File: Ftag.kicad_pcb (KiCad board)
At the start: 2 copper layers, 34.9 x 29.2 mm, 25 parts, among them P1 USB_OTG, P2 CONN_10X2, U1 FT232H, U2 TXB0108, X1 12 MHz

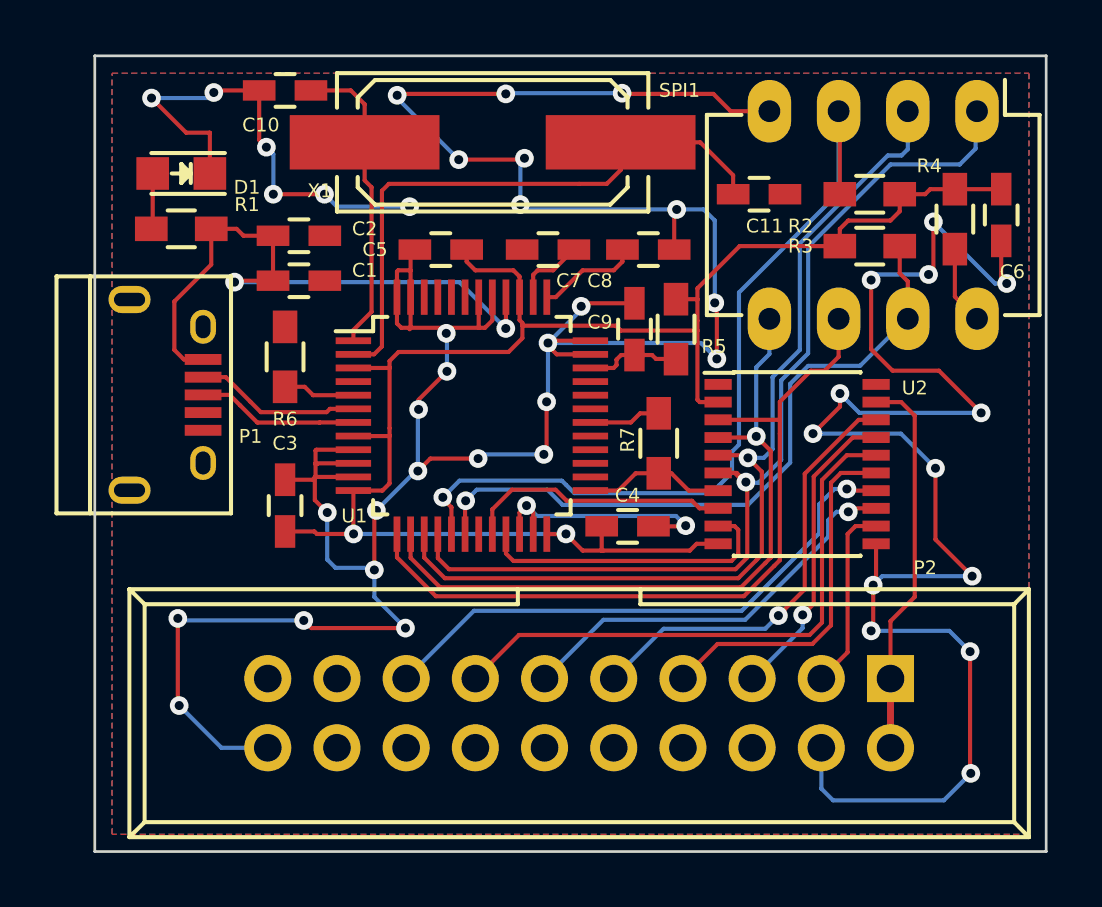
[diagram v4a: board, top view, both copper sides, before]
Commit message: Finished PCB layout
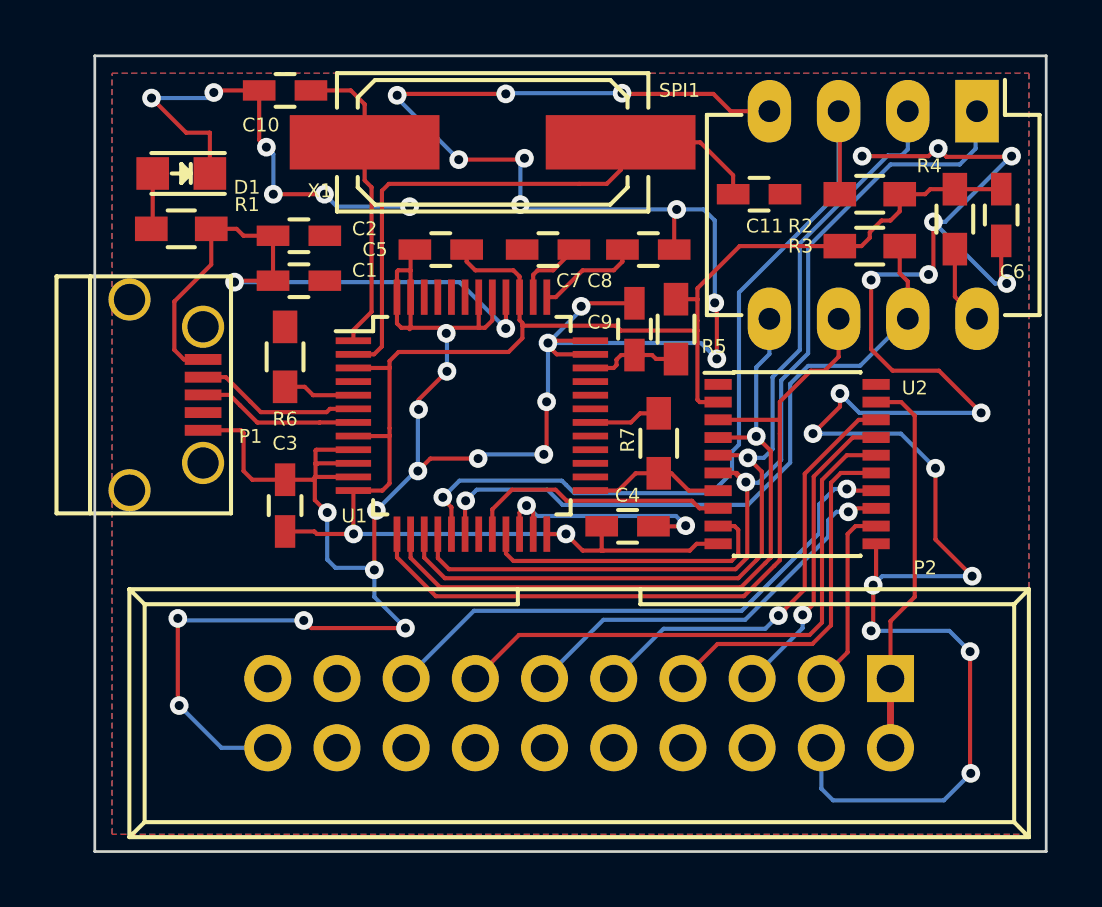
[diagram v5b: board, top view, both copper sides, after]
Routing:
- net GND: track 197.5 -> 211.7 mm, vias 46 -> 49
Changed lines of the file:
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@@
     (thickness 1.6)
     (drawings 17)
-    (tracks 542)
+    (tracks 562)
     (zones 0)
     (modules 25)
@@
     (mod_text_size 1 1)
     (mod_text_width 0.15)
-    (pad_size 5.4991 1.99898)
-    (pad_drill 0)
+    (pad_size 2.3 1.6)
+    (pad_drill 0.8)
     (pad_to_mask_clearance 0)
     (aux_axis_origin 0 0)
-    (visible_elements FFFFFFFF)
+    (visible_elements FFFFFF7F)
     (pcbplotparams
       (layerselection 0x010f0_80000001)
@@
     (pad 5 smd rect (at 1.2991 -1.56254) (size 1.35 0.4) (layers F.Cu F.Paste F.Mask)
       (net 2 GND))
-    (pad 6 thru_hole oval (at -2.5009 -1.56254) (size 0.95 1.25) (drill oval 0.55 0.85) (layers *.Cu *.Mask F.SilkS)
-      (net 2 GND))
-    (pad 6 thru_hole oval (at 2.4991 -1.56254) (size 0.95 1.25) (drill oval 0.55 0.85) (layers *.Cu *.Mask F.SilkS)
-      (net 2 GND))
-    (pad 6 thru_hole oval (at -3.5009 1.13746) (size 1.55 1) (drill oval 1.15 0.5) (layers *.Cu *.Mask F.SilkS)
-      (net 2 GND))
-    (pad 6 thru_hole oval (at 3.4991 1.13746) (size 1.55 1) (drill oval 1.15 0.5) (layers *.Cu *.Mask F.SilkS)
+    (pad 6 thru_hole circle (at -2.5009 -1.56254) (size 1.55 1.55) (drill 1.15) (layers *.Cu *.Mask F.SilkS)
+      (net 2 GND))
+    (pad 6 thru_hole circle (at 2.4991 -1.56254) (size 1.55 1.55) (drill 1.15) (layers *.Cu *.Mask F.SilkS)
+      (net 2 GND))
+    (pad 6 thru_hole circle (at -3.5009 1.13746) (size 1.55 1.55) (drill 1.15) (layers *.Cu *.Mask F.SilkS)
+      (net 2 GND))
+    (pad 6 thru_hole circle (at 3.4991 1.13746) (size 1.55 1.55) (drill 1.15) (layers *.Cu *.Mask F.SilkS)
       (net 2 GND))
   )
@@
     (fp_line (start 0.135 9.915) (end 7.485 9.915) (layer F.SilkS) (width 0.15))
     (fp_line (start 0.135 -1.025) (end -1.15 -1.025) (layer F.SilkS) (width 0.15))
-    (pad 1 thru_hole oval (at 0 0 270) (size 2.3 1.6) (drill 0.8) (layers *.Cu *.Mask F.SilkS)
+    (pad 1 thru_hole rect (at 0 0 270) (size 2.3 1.6) (drill 0.8) (layers *.Cu *.Mask F.SilkS)
       (net 24 /CTS/TMS/CS))
     (pad 2 thru_hole oval (at 0 2.54 270) (size 2.3 1.6) (drill 0.8) (layers *.Cu *.Mask F.SilkS)
@@
   (segment (start 148.336 75.184) (end 148.082 74.93) (width 0.1524) (layer F.Cu) (net 1))
   (segment (start 149.418 76.835) (end 149.418 75.184) (width 0.1524) (layer F.Cu) (net 1))
+  (segment (start 173.8376 71.9836) (end 173.7614 71.9836) (width 0.1524) (layer F.Cu) (net 2))
+  (via (at 171.0436 72.263) (size 0.6858) (drill 0.3302) (layers F.Cu B.Cu) (net 2))
+  (segment (start 173.482 72.263) (end 171.0436 72.263) (width 0.1524) (layer F.Cu) (net 2))
+  (segment (start 173.7614 71.9836) (end 173.482 72.263) (width 0.1524) (layer F.Cu) (net 2))
+  (segment (start 173.6598 74.676) (end 174.0916 74.676) (width 0.1524) (layer B.Cu) (net 2))
+  (segment (start 173.8376 71.9836) (end 173.8376 71.9582) (width 0.1524) (layer B.Cu) (net 2))
+  (via (at 173.8376 71.9836) (size 0.6858) (drill 0.3302) (layers F.Cu B.Cu) (net 2))
+  (segment (start 174.1424 72.2884) (end 173.8376 71.9836) (width 0.1524) (layer F.Cu) (net 2))
+  (segment (start 176.5046 72.2884) (end 174.1424 72.2884) (width 0.1524) (layer F.Cu) (net 2))
+  (segment (start 176.53 72.263) (end 176.5046 72.2884) (width 0.1524) (layer F.Cu) (net 2))
+  (via (at 176.53 72.263) (size 0.6858) (drill 0.3302) (layers F.Cu B.Cu) (net 2))
+  (segment (start 176.5046 72.263) (end 176.53 72.263) (width 0.1524) (layer B.Cu) (net 2))
+  (segment (start 174.0916 74.676) (end 176.5046 72.263) (width 0.1524) (layer B.Cu) (net 2))
+  (segment (start 152.368 83.038) (end 151.0084 83.038) (width 0.1524) (layer F.Cu) (net 2))
+  (segment (start 151.0084 83.038) (end 150.9776 83.0688) (width 0.1524) (layer F.Cu) (net 2))
+  (segment (start 150.9776 83.0688) (end 150.9776 83.566) (width 0.1524) (layer F.Cu) (net 2))
+  (segment (start 146.85054 82.3251) (end 148.2381 82.3251) (width 0.1524) (layer F.Cu) (net 2))
+  (segment (start 148.656 84.14) (end 149.86 84.14) (width 0.1524) (layer F.Cu) (net 2))
+  (segment (start 148.336 83.82) (end 148.656 84.14) (width 0.1524) (layer F.Cu) (net 2))
+  (segment (start 148.336 82.423) (end 148.336 83.82) (width 0.1524) (layer F.Cu) (net 2))
+  (segment (start 148.2381 82.3251) (end 148.336 82.423) (width 0.1524) (layer F.Cu) (net 2))
   (via (at 175.4124 81.6864) (size 0.6858) (drill 0.3302) (layers F.Cu B.Cu) (net 2))
   (via (at 175.0822 87.6808) (size 0.6858) (drill 0.3302) (layers F.Cu B.Cu) (net 2))
@@
   (segment (start 150.9522 84.038) (end 150.9882 84.038) (width 0.1524) (layer F.Cu) (net 2))
   (segment (start 150.9882 84.038) (end 150.9776 84.0486) (width 0.1524) (layer F.Cu) (net 2))
-  (segment (start 152.368 83.038) (end 151.0084 83.038) (width 0.1524) (layer F.Cu) (net 2))
   (segment (start 150.8862 84.14) (end 149.86 84.14) (width 0.1524) (layer F.Cu) (net 2))
   (segment (start 150.9776 84.0486) (end 150.8862 84.14) (width 0.1524) (layer F.Cu) (net 2))
-  (segment (start 150.9776 83.0688) (end 150.9776 83.566) (width 0.1524) (layer F.Cu) (net 2))
   (segment (start 150.9776 83.566) (end 150.9776 84.0486) (width 0.1524) (layer F.Cu) (net 2))
-  (segment (start 151.0084 83.038) (end 150.9776 83.0688) (width 0.1524) (layer F.Cu) (net 2))
+  (segment (start 170.223 75.565) (end 171.0182 75.565) (width 0.1524) (layer F.Cu) (net 3))
+  (segment (start 171.323 75.057) (end 171.7548 74.6252) (width 0.1524) (layer F.Cu) (net 3))
+  (segment (start 171.323 75.2602) (end 171.323 75.057) (width 0.1524) (layer F.Cu) (net 3))
+  (segment (start 171.0182 75.565) (end 171.323 75.2602) (width 0.1524) (layer F.Cu) (net 3))
   (segment (start 174.4472 73.4744) (end 176.1466 73.4744) (width 0.1524) (layer F.Cu) (net 3))
   (segment (start 176.1466 73.4744) (end 176.149 73.472) (width 0.1524) (layer F.Cu) (net 3))
@@
   (segment (start 160.1658 86.138) (end 159.468 86.138) (width 0.1524) (layer F.Cu) (net 3))
   (segment (start 160.1724 86.1314) (end 160.1658 86.138) (width 0.1524) (layer F.Cu) (net 3))
-  (segment (start 170.223 75.565) (end 170.223 74.9378) (width 0.1524) (layer F.Cu) (net 3))
   (segment (start 172.423 74.2872) (end 172.423 73.66) (width 0.1524) (layer F.Cu) (net 3))
   (segment (start 172.085 74.6252) (end 172.423 74.2872) (width 0.1524) (layer F.Cu) (net 3))
-  (segment (start 170.5356 74.6252) (end 172.085 74.6252) (width 0.1524) (layer F.Cu) (net 3))
-  (segment (start 170.223 74.9378) (end 170.5356 74.6252) (width 0.1524) (layer F.Cu) (net 3))
+  (segment (start 171.7548 74.6252) (end 172.085 74.6252) (width 0.1524) (layer F.Cu) (net 3))
   (segment (start 152.368 82.538) (end 153.6954 82.538) (width 0.1524) (layer F.Cu) (net 3))
   (segment (start 153.67 82.5246) (end 153.6954 82.5246) (width 0.1524) (layer F.Cu) (net 3))
@@
     (connect_pads (clearance 0.1524))
     (min_thickness 0.1524)
-    (fill yes (arc_segments 16) (thermal_gap 0.508) (thermal_bridge_width 0.508))
+    (fill yes (arc_segments 16) (thermal_gap 0.508) (thermal_bridge_width 0.254))
     (polygon
       (pts
@@
     (connect_pads (clearance 0.1524))
     (min_thickness 0.1524)
-    (fill yes (arc_segments 16) (thermal_gap 0.508) (thermal_bridge_width 0.508))
+    (fill yes (arc_segments 16) (thermal_gap 0.508) (thermal_bridge_width 0.254))
     (polygon
       (pts
